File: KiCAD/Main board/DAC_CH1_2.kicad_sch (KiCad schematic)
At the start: 73 parts, among them U1 LM4562, U1 PCM1789, U3 OPA1632DR, U4 OPA1632DR

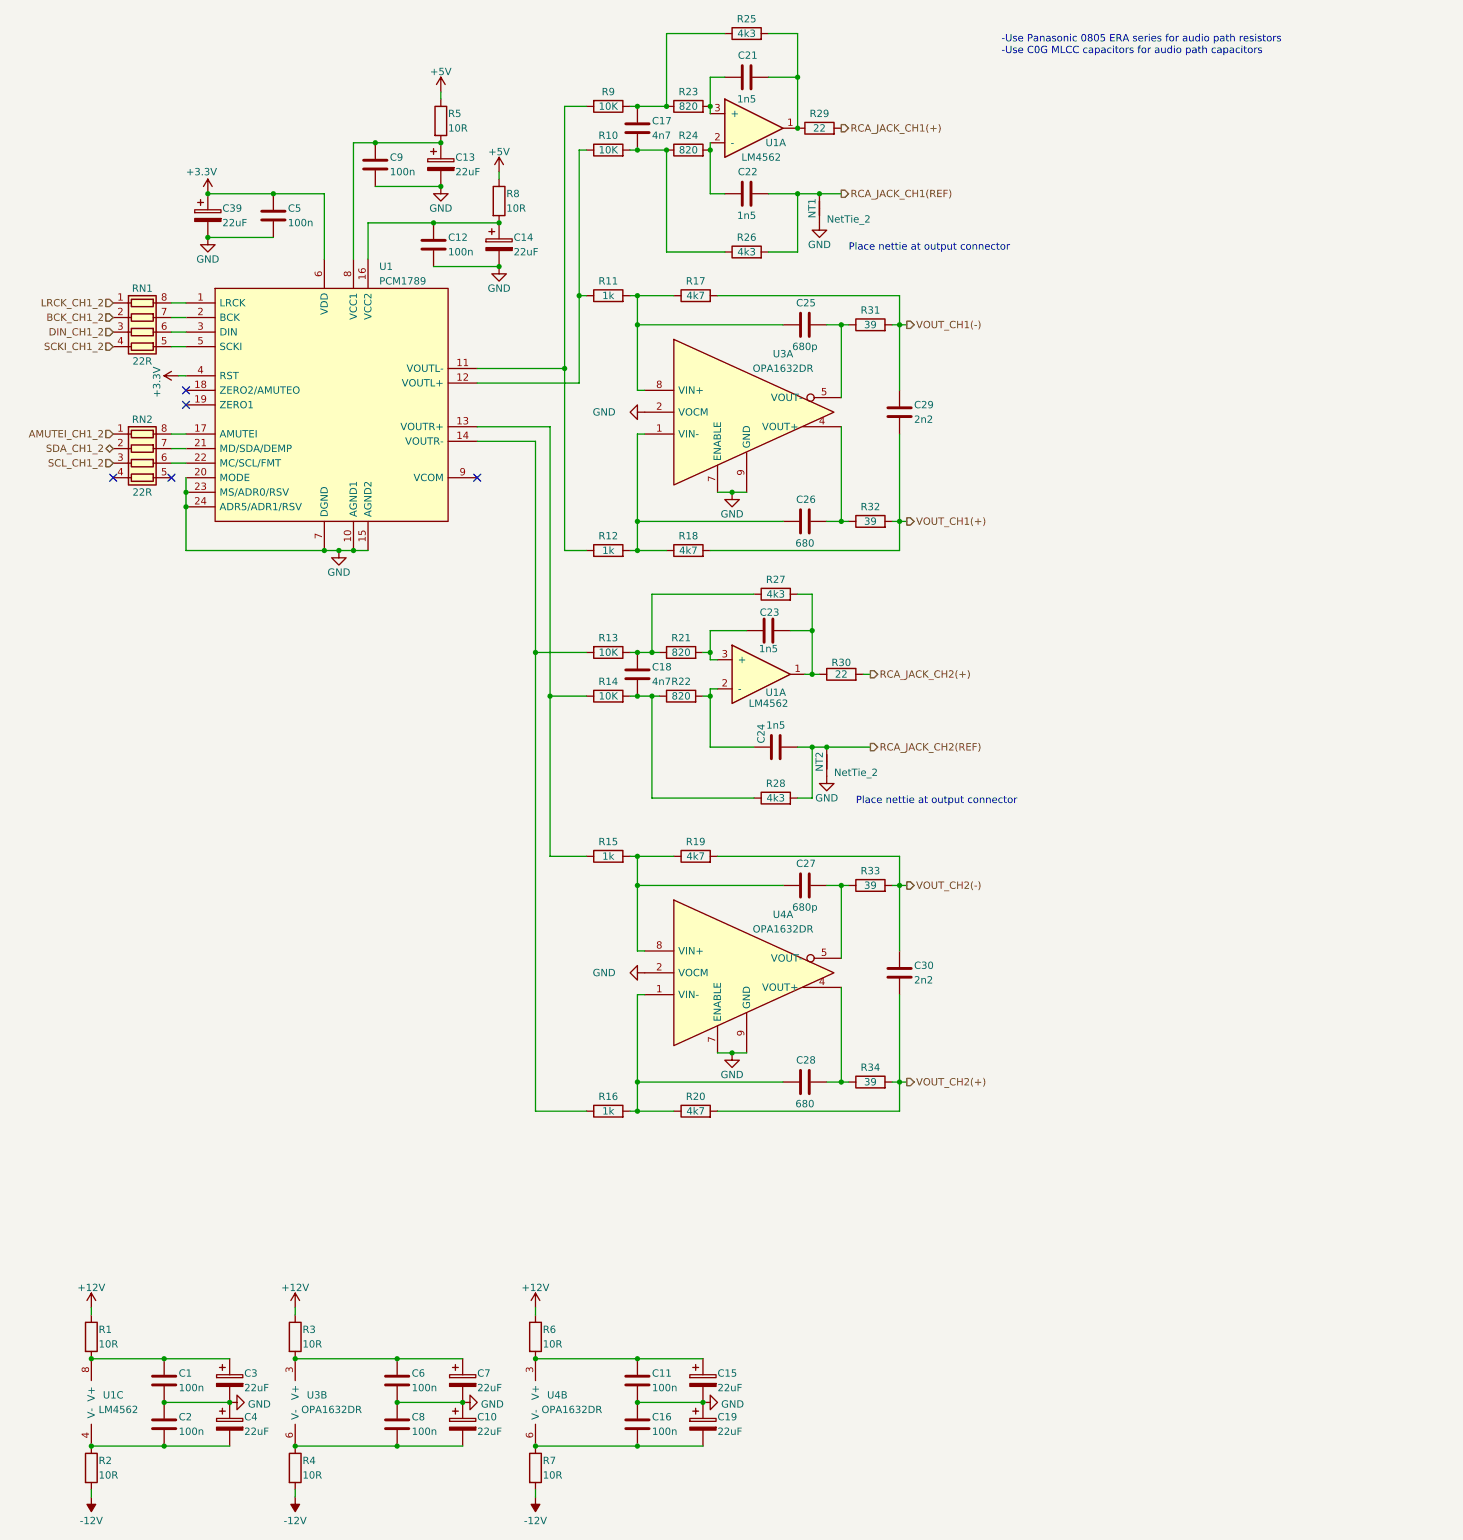
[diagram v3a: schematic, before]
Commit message: Worked on main board schematic and PCB, added symbols to symbol library
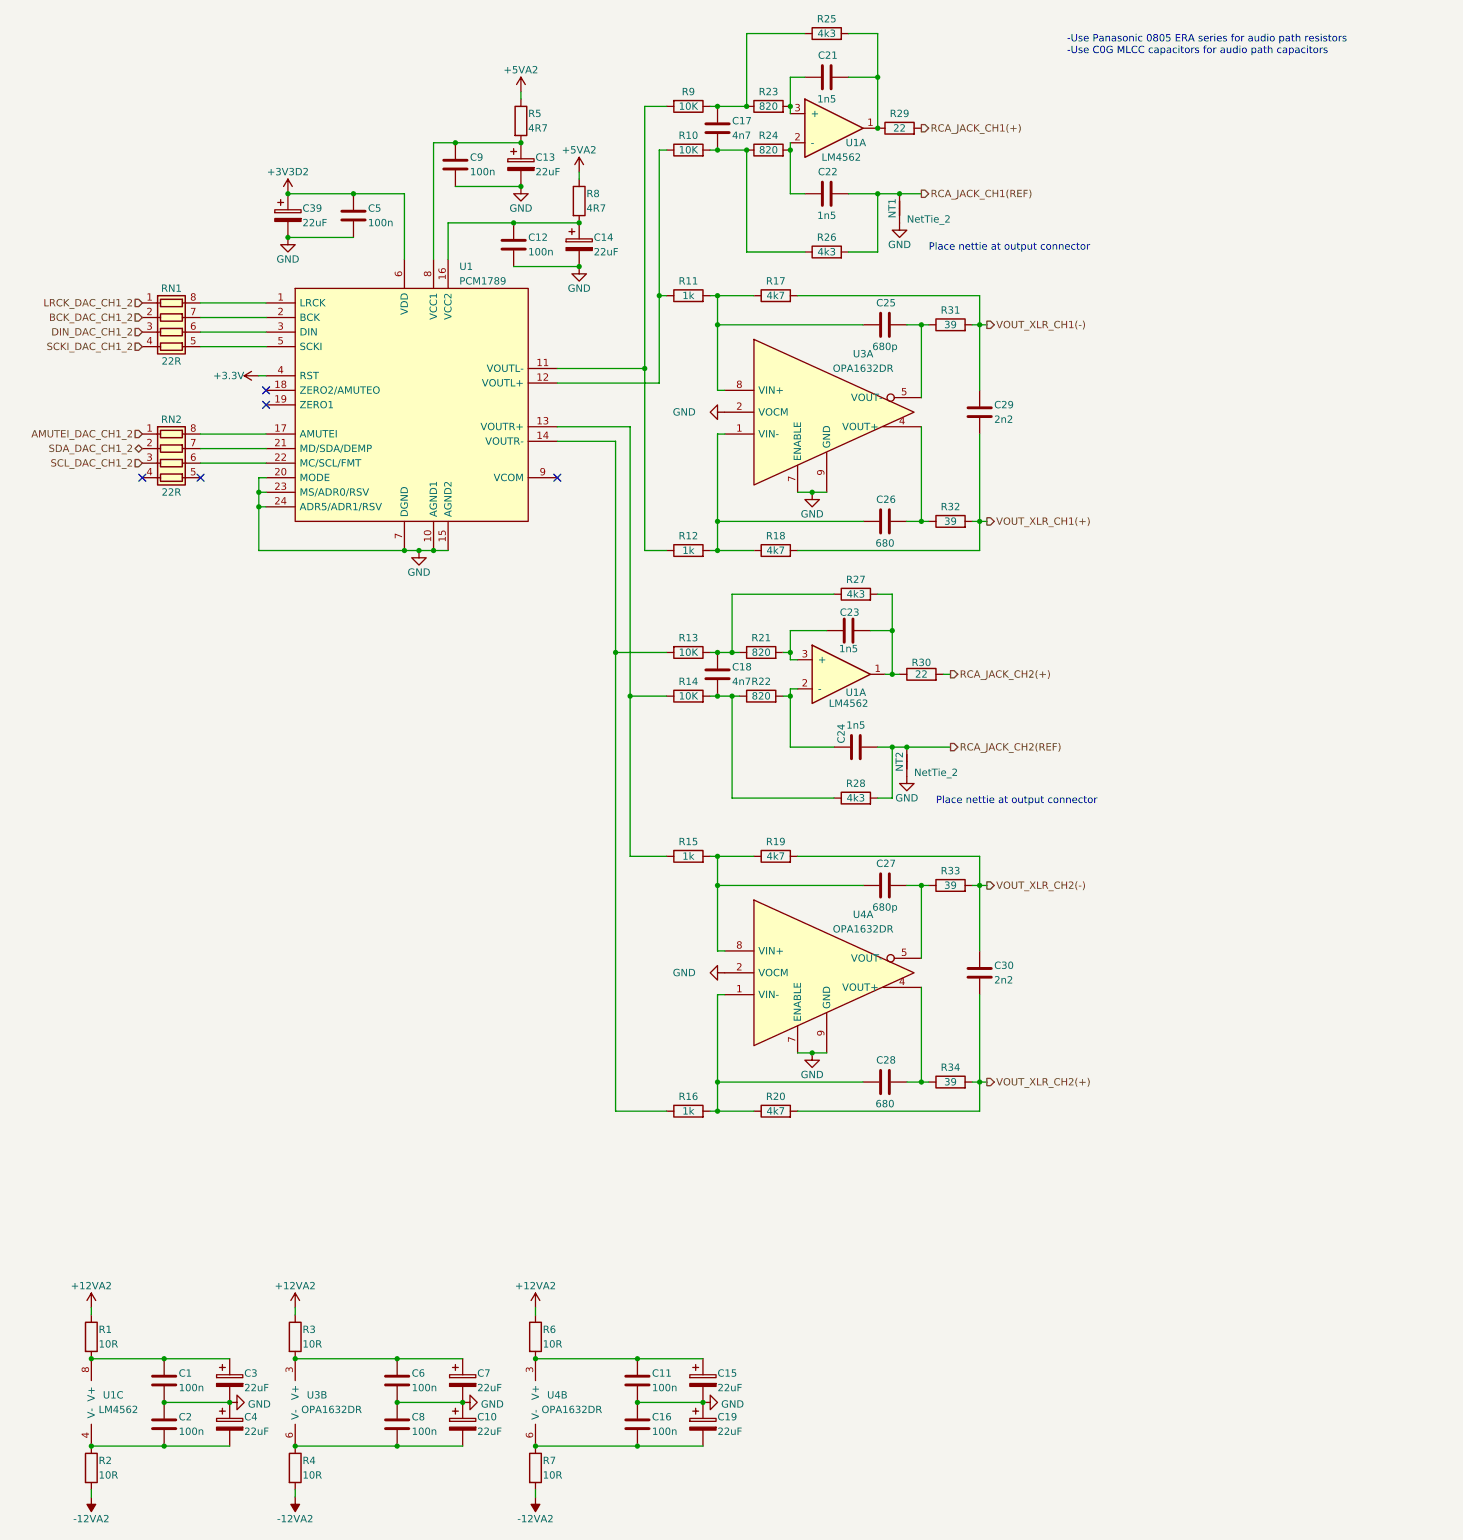
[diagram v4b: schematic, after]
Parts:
- R5, R8: value 10R -> 4R7
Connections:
- net +3.3V: no longer C39.1, C5.1, U1.6 (VDD)
- net +12V renamed +12VA2
- net +5V renamed +5VA2
- net -12V renamed -12VA2
- net AMUTEI_CH1_2 renamed AMUTEI_DAC_CH1_2
- net BCK_CH1_2 renamed BCK_DAC_CH1_2
- net DIN_CH1_2 renamed DIN_DAC_CH1_2
- net LRCK_CH1_2 renamed LRCK_DAC_CH1_2
- net SCKI_CH1_2 renamed SCKI_DAC_CH1_2
- net SCL_CH1_2 renamed SCL_DAC_CH1_2
- net SDA_CH1_2 renamed SDA_DAC_CH1_2
- net VOUT_CH1(+) renamed VOUT_XLR_CH1(+)
- net VOUT_CH1(-) renamed VOUT_XLR_CH1(-)
- net VOUT_CH2(+) renamed VOUT_XLR_CH2(+)
- net VOUT_CH2(-) renamed VOUT_XLR_CH2(-)
- new net +3V3D2: C39.1, C5.1, U1.6 (VDD)
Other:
- moved on the sheet: C12, C13, C14, C17, C18, C21, C22, C23, C24, C25, C26, C27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

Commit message: Worked on main board design
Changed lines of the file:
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@@
-    (stroke (width 0) (type default))
-  )
-  (wire (pts (xy 59.69 238.76) (xy 59.69 240.03))
     (stroke (width 0) (type default))
   )
@@
     (stroke (width 0) (type default))
   )
-  (wire (pts (xy 24.13 238.76) (xy 24.13 240.03))
-    (stroke (width 0) (type default))
-  )
   (wire (pts (xy 147.32 204.47) (xy 179.07 204.47))
     (stroke (width 0) (type default))
@@
     (stroke (width 0) (type default))
   )
-  (wire (pts (xy 24.13 270.51) (xy 24.13 271.78))
-    (stroke (width 0) (type default))
-  )
   (wire (pts (xy 161.29 140.97) (xy 163.83 140.97))
     (stroke (width 0) (type default))
@@
     (stroke (width 0) (type default))
   )
-  (wire (pts (xy 101.6 270.51) (xy 101.6 271.78))
-    (stroke (width 0) (type default))
-  )
   (wire (pts (xy 133.35 176.53) (xy 134.62 176.53))
     (stroke (width 0) (type default))
@@
     (stroke (width 0) (type default))
   )
-  (wire (pts (xy 101.6 238.76) (xy 101.6 240.03))
-    (stroke (width 0) (type default))
-  )
   (wire (pts (xy 138.43 54.61) (xy 138.43 36.83))
     (stroke (width 0) (type default))
@@
   )
   (wire (pts (xy 168.91 101.6) (xy 168.91 85.09))
-    (stroke (width 0) (type default))
-  )
-  (wire (pts (xy 59.69 270.51) (xy 59.69 271.78))
     (stroke (width 0) (type default))
   )
@@
     )
   )
-  (symbol (lib_id "Audio-DSP:+12VA2") (at 101.6 238.76 0) (unit 1)
+  (symbol (lib_id "Audio-DSP:+12VA2") (at 101.6 240.03 0) (unit 1)
     (in_bom no) (on_board no) (dnp no) (fields_autoplaced)
-    (property "Reference" "#PWR057" (at 101.6 241.3 0)
-      (effects (font (size 1.27 1.27)) hide)
-    )
-    (property "Value" "+12VA2" (at 101.6 234.95 0)
-      (effects (font (size 1.27 1.27)))
-    )
-    (property "Footprint" "" (at 101.6 238.76 0)
-      (effects (font (size 1.27 1.27)) hide)
-    )
-    (property "Datasheet" "" (at 101.6 238.76 0)
+    (property "Reference" "#PWR057" (at 101.6 242.57 0)
+      (effects (font (size 1.27 1.27)) hide)
+    )
+    (property "Value" "+12VA2" (at 101.6 236.22 0)
+      (effects (font (size 1.27 1.27)))
+    )
+    (property "Footprint" "" (at 101.6 240.03 0)
+      (effects (font (size 1.27 1.27)) hide)
+    )
+    (property "Datasheet" "" (at 101.6 240.03 0)
       (effects (font (size 1.27 1.27)) hide)
     )
@@
     )
   )
-  (symbol (lib_id "Audio-DSP:+12VA2") (at 24.13 238.76 0) (unit 1)
+  (symbol (lib_id "Audio-DSP:+12VA2") (at 24.13 240.03 0) (unit 1)
     (in_bom no) (on_board no) (dnp no) (fields_autoplaced)
-    (property "Reference" "#PWR052" (at 24.13 241.3 0)
-      (effects (font (size 1.27 1.27)) hide)
-    )
-    (property "Value" "+12VA2" (at 24.13 234.95 0)
-      (effects (font (size 1.27 1.27)))
-    )
-    (property "Footprint" "" (at 24.13 238.76 0)
-      (effects (font (size 1.27 1.27)) hide)
-    )
-    (property "Datasheet" "" (at 24.13 238.76 0)
+    (property "Reference" "#PWR052" (at 24.13 242.57 0)
+      (effects (font (size 1.27 1.27)) hide)
+    )
+    (property "Value" "+12VA2" (at 24.13 236.22 0)
+      (effects (font (size 1.27 1.27)))
+    )
+    (property "Footprint" "" (at 24.13 240.03 0)
+      (effects (font (size 1.27 1.27)) hide)
+    )
+    (property "Datasheet" "" (at 24.13 240.03 0)
       (effects (font (size 1.27 1.27)) hide)
     )
@@
     )
   )
-  (symbol (lib_id "Audio-DSP:-12VA2") (at 24.13 271.78 180) (unit 1)
+  (symbol (lib_id "Audio-DSP:-12VA2") (at 24.13 270.51 180) (unit 1)
     (in_bom no) (on_board no) (dnp no)
-    (property "Reference" "#PWR053" (at 24.13 269.24 0)
-      (effects (font (size 1.27 1.27)) hide)
-    )
-    (property "Value" "-12VA2" (at 24.13 275.59 0)
-      (effects (font (size 1.27 1.27)))
-    )
-    (property "Footprint" "" (at 24.13 271.78 0)
-      (effects (font (size 1.27 1.27)) hide)
-    )
-    (property "Datasheet" "" (at 24.13 271.78 0)
+    (property "Reference" "#PWR053" (at 24.13 267.97 0)
+      (effects (font (size 1.27 1.27)) hide)
+    )
+    (property "Value" "-12VA2" (at 24.13 274.32 0)
+      (effects (font (size 1.27 1.27)))
+    )
+    (property "Footprint" "" (at 24.13 270.51 0)
+      (effects (font (size 1.27 1.27)) hide)
+    )
+    (property "Datasheet" "" (at 24.13 270.51 0)
       (effects (font (size 1.27 1.27)) hide)
     )
@@
     )
   )
-  (symbol (lib_id "Audio-DSP:-12VA2") (at 101.6 271.78 180) (unit 1)
+  (symbol (lib_id "Audio-DSP:-12VA2") (at 101.6 270.51 180) (unit 1)
     (in_bom no) (on_board no) (dnp no)
-    (property "Reference" "#PWR059" (at 101.6 269.24 0)
-      (effects (font (size 1.27 1.27)) hide)
-    )
-    (property "Value" "-12VA2" (at 101.6 275.59 0)
-      (effects (font (size 1.27 1.27)))
-    )
-    (property "Footprint" "" (at 101.6 271.78 0)
-      (effects (font (size 1.27 1.27)) hide)
-    )
-    (property "Datasheet" "" (at 101.6 271.78 0)
+    (property "Reference" "#PWR059" (at 101.6 267.97 0)
+      (effects (font (size 1.27 1.27)) hide)
+    )
+    (property "Value" "-12VA2" (at 101.6 274.32 0)
+      (effects (font (size 1.27 1.27)))
+    )
+    (property "Footprint" "" (at 101.6 270.51 0)
+      (effects (font (size 1.27 1.27)) hide)
+    )
+    (property "Datasheet" "" (at 101.6 270.51 0)
       (effects (font (size 1.27 1.27)) hide)
     )
@@
     )
   )
-  (symbol (lib_id "Audio-DSP:+12VA2") (at 59.69 238.76 0) (unit 1)
+  (symbol (lib_id "Audio-DSP:+12VA2") (at 59.69 240.03 0) (unit 1)
     (in_bom no) (on_board no) (dnp no) (fields_autoplaced)
-    (property "Reference" "#PWR056" (at 59.69 241.3 0)
-      (effects (font (size 1.27 1.27)) hide)
-    )
-    (property "Value" "+12VA2" (at 59.69 234.95 0)
-      (effects (font (size 1.27 1.27)))
-    )
-    (property "Footprint" "" (at 59.69 238.76 0)
-      (effects (font (size 1.27 1.27)) hide)
-    )
-    (property "Datasheet" "" (at 59.69 238.76 0)
+    (property "Reference" "#PWR056" (at 59.69 242.57 0)
+      (effects (font (size 1.27 1.27)) hide)
+    )
+    (property "Value" "+12VA2" (at 59.69 236.22 0)
+      (effects (font (size 1.27 1.27)))
+    )
+    (property "Footprint" "" (at 59.69 240.03 0)
+      (effects (font (size 1.27 1.27)) hide)
+    )
+    (property "Datasheet" "" (at 59.69 240.03 0)
       (effects (font (size 1.27 1.27)) hide)
     )
@@
     )
   )
-  (symbol (lib_id "Audio-DSP:-12VA2") (at 59.69 271.78 180) (unit 1)
+  (symbol (lib_id "Audio-DSP:-12VA2") (at 59.69 270.51 180) (unit 1)
     (in_bom no) (on_board no) (dnp no)
-    (property "Reference" "#PWR058" (at 59.69 269.24 0)
-      (effects (font (size 1.27 1.27)) hide)
-    )
-    (property "Value" "-12VA2" (at 59.69 275.59 0)
-      (effects (font (size 1.27 1.27)))
-    )
-    (property "Footprint" "" (at 59.69 271.78 0)
-      (effects (font (size 1.27 1.27)) hide)
-    )
-    (property "Datasheet" "" (at 59.69 271.78 0)
-      (effects (font (size 1.27 1.27)) hide)
-    )
+    (property "Reference" "#PWR058" (at 59.69 267.97 0)
+      (effects (font (size 1.27 1.27)) hide)
+    )
+    (property "Value" "-12VA2" (at 59.69 274.32 0)
+      (effects (font (size 1.27 1.27)))
+    )
+    (property "Footprint" "" (at 59.69 270.51 0)
+      (effects (font (size 1.27 1.27)) hide)
+    )
+    (property "Datasheet" "" (at 59.69 270.51 0)
+      (effects (font (size 1.27 1.27)) hide)
+    )

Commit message: Worked in main board
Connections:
- net +3.3V is gone; now on net +3V3D2: U1.4 (RST)
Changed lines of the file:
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@@
-    (stroke (width 0) (type default))
-  )
-  (wire (pts (xy 53.34 76.2) (xy 54.61 76.2))
     (stroke (width 0) (type default))
   )
@@
         (path "/2f8cbac6-fd11-4240-8e40-3bb6952a0324/03c234da-ad6d-41dc-b0ec-5880e5376fd2"
           (reference "#PWR0136") (unit 1)
+        )
+      )
+    )
+  )
+  (symbol (lib_id "Audio_DSP:+3V3D2") (at 54.61 76.2 90) (unit 1)
+    (in_bom no) (on_board no) (dnp no)
+    (property "Reference" "#PWR0106" (at 57.15 76.2 0)
+      (effects (font (size 1.27 1.27)) hide)
+    )
+    (property "Value" "+3V3D2" (at 52.07 76.2 90)
+      (effects (font (size 1.27 1.27)) (justify left))
+    )
+    (property "Footprint" "" (at 54.61 76.2 0)
+      (effects (font (size 1.27 1.27)) hide)
+    )
+    (property "Datasheet" "" (at 54.61 76.2 0)
+      (effects (font (size 1.27 1.27)) hide)
+    )
+    (pin "1")
+    (instances
+      (project "Main board"
+        (path "/2f8cbac6-fd11-4240-8e40-3bb6952a0324/fc272ee1-9060-465b-85c1-b8364d68deb3"
+          (reference "#PWR0106") (unit 1)
+        )
+        (path "/2f8cbac6-fd11-4240-8e40-3bb6952a0324/05d59304-dfac-45e1-85e6-83cda4d81484"
+          (reference "#PWR0174") (unit 1)
+        )
+        (path "/2f8cbac6-fd11-4240-8e40-3bb6952a0324/03c234da-ad6d-41dc-b0ec-5880e5376fd2"
+          (reference "#PWR046") (unit 1)
         )
       )
@@
         )
       )
-    )
-  )
-  (symbol (lib_id "power:+3.3V") (at 53.34 76.2 90) (unit 1)
-    (in_bom yes) (on_board yes) (dnp no)
-    (property "Reference" "#PWR0137" (at 57.15 76.2 0)
-      (effects (font (size 1.27 1.27)) hide)
-    )
-    (property "Value" "+3.3V" (at 50.8 76.2 90)
-      (effects (font (size 1.27 1.27)) (justify left))
-    )
-    (property "Footprint" "" (at 53.34 76.2 0)
-      (effects (font (size 1.27 1.27)) hide)
-    )
-    (property "Datasheet" "" (at 53.34 76.2 0)
-      (effects (font (size 1.27 1.27)) hide)
-    )
-    (pin "1")
-    (instances
-      (project "Main board"
-        (path "/2f8cbac6-fd11-4240-8e40-3bb6952a0324/03c234da-ad6d-41dc-b0ec-5880e5376fd2"
-          (reference "#PWR0137") (unit 1)
-        )
-      )

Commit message: Worked on main board schematic
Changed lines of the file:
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@@
-    (stroke (width 0) (type default))
-  )
-  (wire (pts (xy 99.06 27.94) (xy 99.06 26.67))
     (stroke (width 0) (type default))
   )
@@
   )
   (wire (pts (xy 133.35 184.15) (xy 133.35 199.39))
-    (stroke (width 0) (type default))
-  )
-  (wire (pts (xy 109.22 41.91) (xy 109.22 40.64))
     (stroke (width 0) (type default))
   )
@@
     )
   )
-  (symbol (lib_id "Audio-DSP:+5VA2") (at 99.06 26.67 0) (unit 1)
+  (symbol (lib_id "Audio-DSP:+5VA2") (at 99.06 27.94 0) (unit 1)
     (in_bom no) (on_board no) (dnp no) (fields_autoplaced)
-    (property "Reference" "#PWR049" (at 99.06 29.21 0)
-      (effects (font (size 1.27 1.27)) hide)
-    )
-    (property "Value" "+5VA2" (at 99.06 22.86 0)
-      (effects (font (size 1.27 1.27)))
-    )
-    (property "Footprint" "" (at 99.06 26.67 0)
-      (effects (font (size 1.27 1.27)) hide)
-    )
-    (property "Datasheet" "" (at 99.06 26.67 0)
+    (property "Reference" "#PWR049" (at 99.06 30.48 0)
+      (effects (font (size 1.27 1.27)) hide)
+    )
+    (property "Value" "+5VA2" (at 99.06 24.13 0)
+      (effects (font (size 1.27 1.27)))
+    )
+    (property "Footprint" "" (at 99.06 27.94 0)
+      (effects (font (size 1.27 1.27)) hide)
+    )
+    (property "Datasheet" "" (at 99.06 27.94 0)
       (effects (font (size 1.27 1.27)) hide)
     )
@@
     )
   )
-  (symbol (lib_id "Audio-DSP:+5VA2") (at 109.22 40.64 0) (unit 1)
+  (symbol (lib_id "Audio-DSP:+5VA2") (at 109.22 41.91 0) (unit 1)
     (in_bom no) (on_board no) (dnp no) (fields_autoplaced)
-    (property "Reference" "#PWR048" (at 109.22 43.18 0)
-      (effects (font (size 1.27 1.27)) hide)
-    )
-    (property "Value" "+5VA2" (at 109.22 36.83 0)
-      (effects (font (size 1.27 1.27)))
-    )
-    (property "Footprint" "" (at 109.22 40.64 0)
-      (effects (font (size 1.27 1.27)) hide)
-    )
-    (property "Datasheet" "" (at 109.22 40.64 0)
+    (property "Reference" "#PWR048" (at 109.22 44.45 0)
+      (effects (font (size 1.27 1.27)) hide)
+    )
+    (property "Value" "+5VA2" (at 109.22 38.1 0)
+      (effects (font (size 1.27 1.27)))
+    )
+    (property "Footprint" "" (at 109.22 41.91 0)
+      (effects (font (size 1.27 1.27)) hide)
+    )
+    (property "Datasheet" "" (at 109.22 41.91 0)
       (effects (font (size 1.27 1.27)) hide)
     )
@@
       (effects (font (size 1.27 1.27)) hide)
     )
-    (property "Value" "GND" (at 129.54 82.55 90)
+    (property "Value" "GND" (at 132.08 82.55 90)
       (effects (font (size 1.27 1.27)) (justify right))
     )
@@
       (effects (font (size 1.27 1.27)) hide)
     )
-    (property "Value" "GND" (at 129.54 180.34 90)
+    (property "Value" "GND" (at 132.08 180.34 90)
       (effects (font (size 1.27 1.27)) (justify right))
     )
